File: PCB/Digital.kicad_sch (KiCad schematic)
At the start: 29 parts, among them IC1 MAX3051ESA+, J1 DE9_Pins_MountingHoles, J2 ICSP, J3 DE9_Plug_MountingHoles, J4 Conn_Coaxial, J6 Conn_01x03, J7 DOOR, J8 WINDOW, U1 PIC18F2580T-I/SO, Y2 ABLS

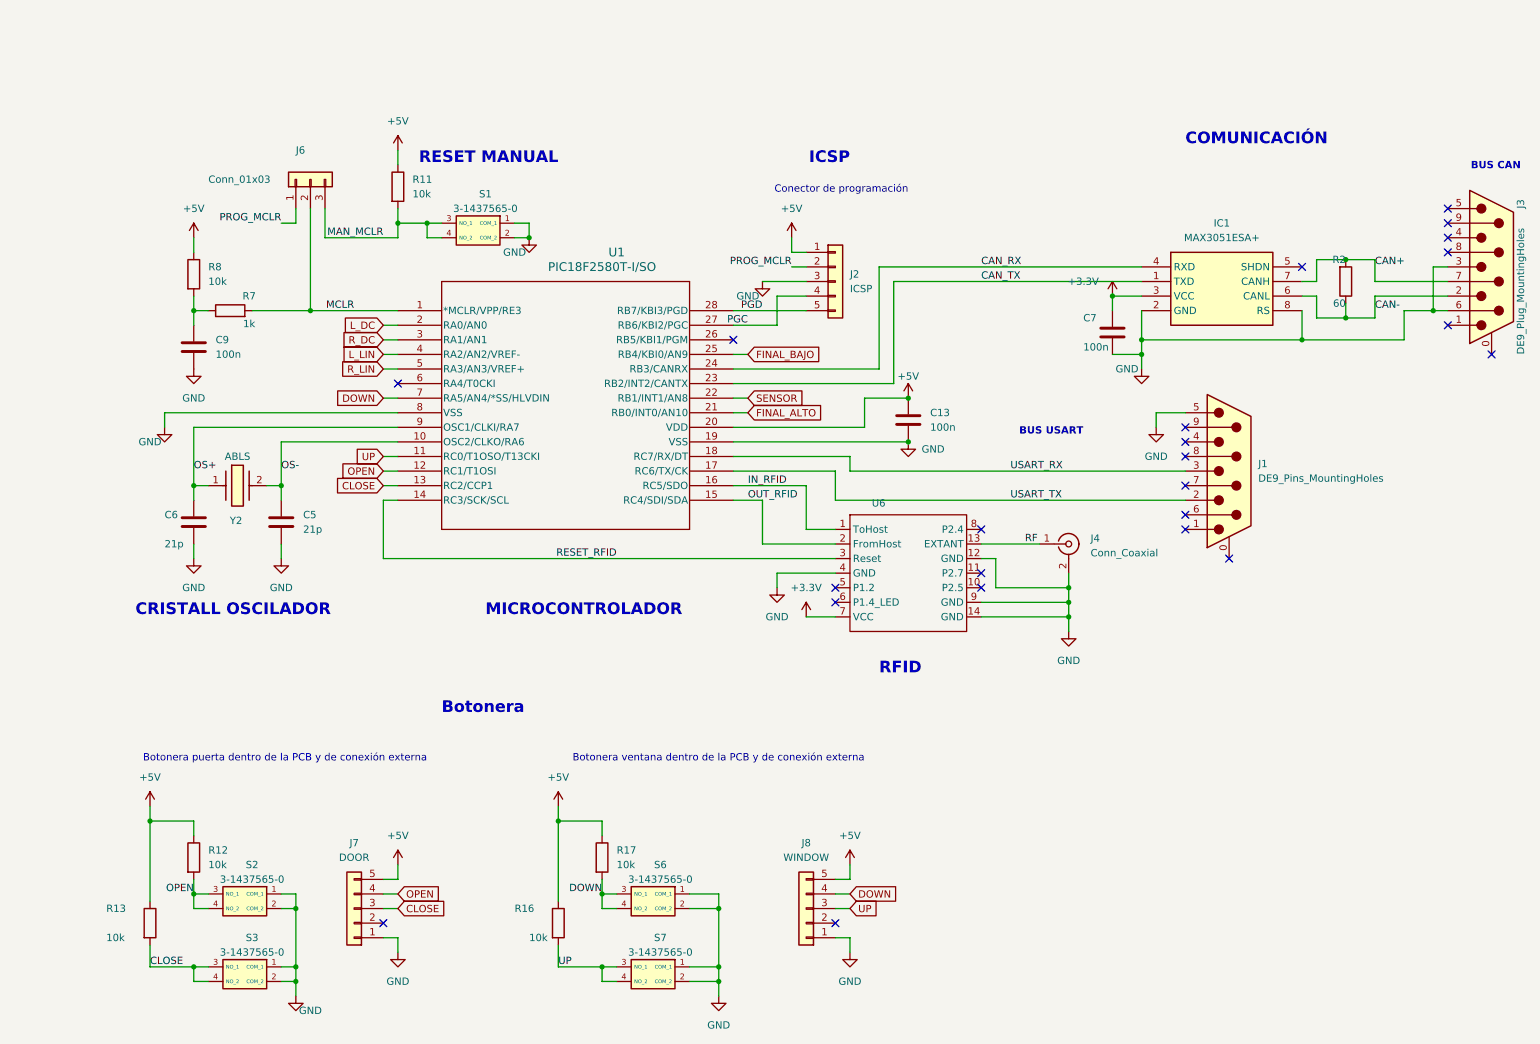
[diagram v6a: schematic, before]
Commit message: Fixed labels and ERC errors
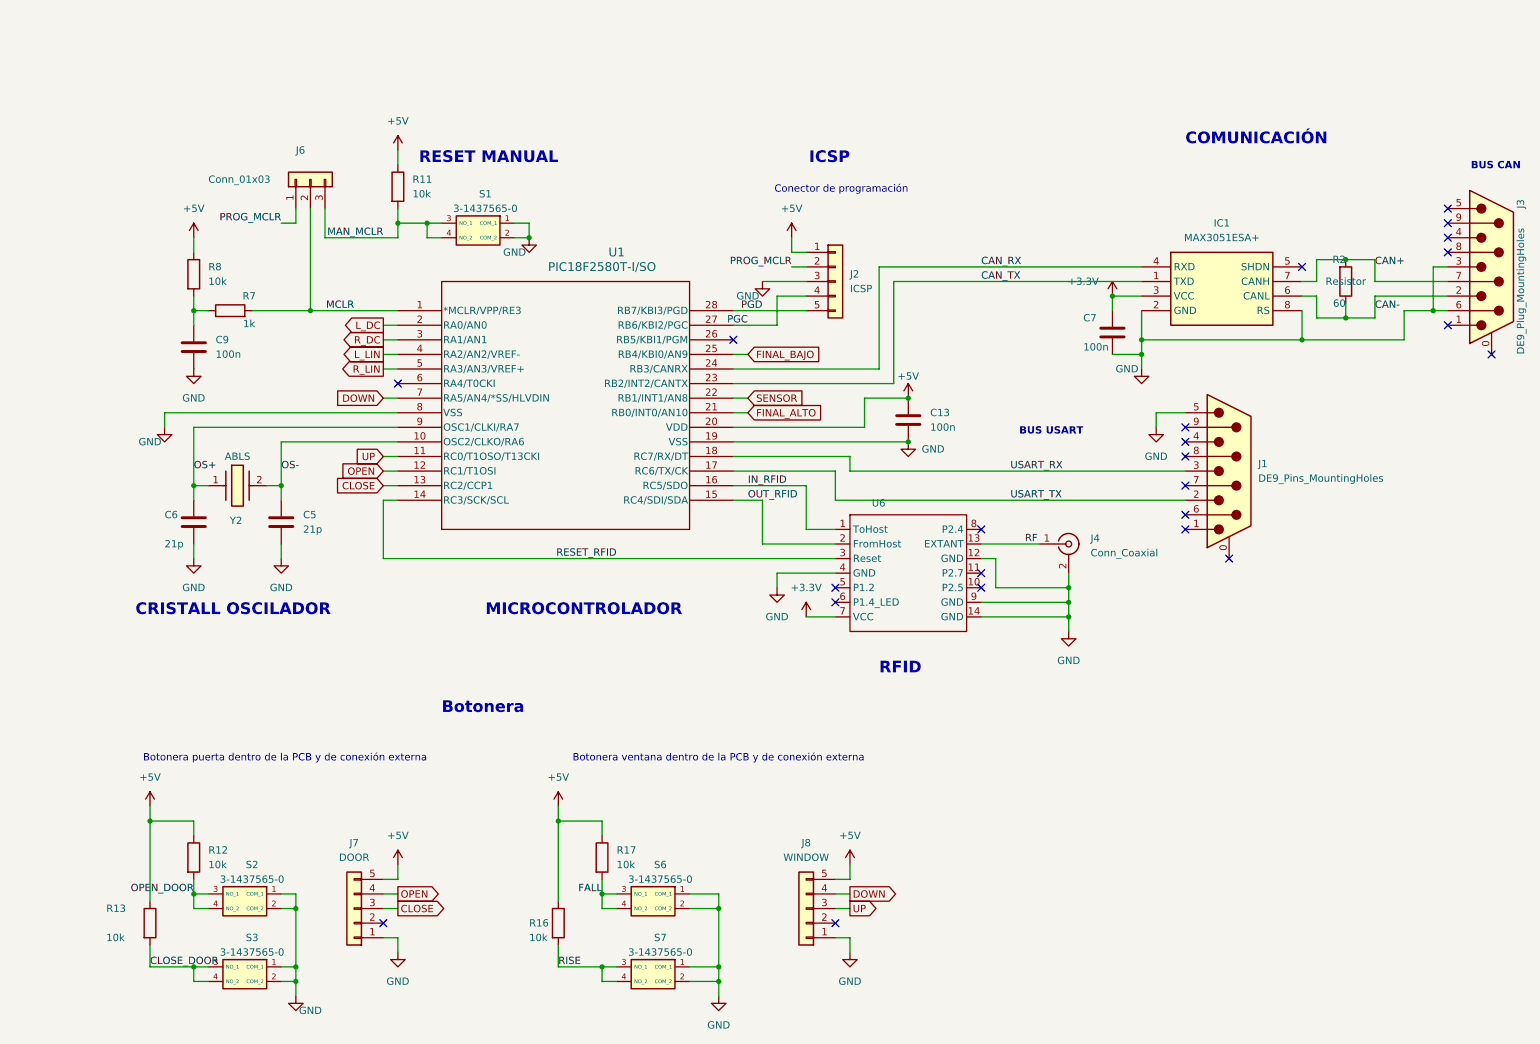
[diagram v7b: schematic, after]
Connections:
- net CLOSE: no longer R13.2, S3.3 (NO_1), S3.4 (NO_2)
- net DOWN: no longer R17.2, S6.3 (NO_1), S6.4 (NO_2)
- net OPEN: no longer R12.2, S2.3 (NO_1), S2.4 (NO_2)
- net UP: no longer R16.2, S7.3 (NO_1), S7.4 (NO_2)
- new net CLOSE_DOOR: R13.2, S3.3 (NO_1), S3.4 (NO_2)
- new net FALL: R17.2, S6.3 (NO_1), S6.4 (NO_2)
- new net OPEN_DOOR: R12.2, S2.3 (NO_1), S2.4 (NO_2)
- new net RISE: R16.2, S7.3 (NO_1), S7.4 (NO_2)
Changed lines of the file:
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@@
 		)
 	)
-	(label "UP"
+	(label "RISE"
 		(at 109.22 180.34 0)
 		(effects
@@
 		)
 	)
-	(label "OPEN"
+	(label "OPEN_DOOR"
 		(at 45.72 167.64 180)
 		(effects
@@
 		)
 	)
-	(label "DOWN"
+	(label "FALL"
 		(at 116.84 167.64 180)
 		(effects
@@
 		)
 	)
-	(label "CLOSE"
+	(label "CLOSE_DOOR"
 		(at 38.1 180.34 0)
 		(effects
@@
 	)
 	(global_label "CLOSE"
-		(shape input)
+		(shape output)
 		(at 81.28 170.18 0)
 		(fields_autoplaced yes)
@@
 	)
 	(global_label "R_DC"
-		(shape input)
+		(shape output)
 		(at 78.74 71.12 180)
 		(fields_autoplaced yes)
@@
 	)
 	(global_label "L_LIN"
-		(shape input)
+		(shape output)
 		(at 78.74 73.66 180)
 		(fields_autoplaced yes)
@@
 	)
 	(global_label "R_LIN"
-		(shape input)
+		(shape output)
 		(at 78.74 76.2 180)
 		(fields_autoplaced yes)
@@
 	)
 	(global_label "UP"
-		(shape input)
+		(shape output)
 		(at 160.02 170.18 0)
 		(fields_autoplaced yes)
@@
 	)
 	(global_label "L_DC"
-		(shape input)
+		(shape output)
 		(at 78.74 68.58 180)
 		(fields_autoplaced yes)
@@
 	)
 	(global_label "DOWN"
-		(shape input)
+		(shape output)
 		(at 160.02 167.64 0)
 		(fields_autoplaced yes)
@@
 	)
 	(global_label "OPEN"
-		(shape input)
+		(shape output)
 		(at 81.28 167.64 0)
 		(fields_autoplaced yes)
@@
 	)
 	(symbol
-		(lib_name "GND_6")
 		(lib_id "power:GND")
 		(at 144.78 60.96 0)
@@
 	)
 	(symbol
-		(lib_name "GND_4")
 		(lib_id "power:GND")
 		(at 198.12 121.92 0)
@@
 			)
 		)
-		(property "Description" ""
+		(property "Description" "Power symbol creates a global label with name \"GND\" , ground"
 			(at 40.64 86.36 0)
 			(effects
@@
 					(size 1.27 1.27)
 				)
+				(hide yes)
 			)
 		)
@@
 			)
 		)
-		(property "Description" ""
+		(property "Description" "Resistor"
 			(at 246.38 60.96 0)
 			(effects
@@
 	)
 	(symbol
-		(lib_name "+5V_1")
 		(lib_id "power:+5V")
 		(at 81.28 162.56 0)
@@
 		(dnp no)
 		(property "Reference" "R16"
-			(at 101.6 170.18 0)
+			(at 104.14 172.72 0)
 			(effects
 				(font
@@
 	)
 	(symbol
-		(lib_name "GND_3")
 		(lib_id "power:GND")
 		(at 213.36 86.36 0)
@@
 	)
 	(symbol
-		(lib_name "GND_5")
 		(lib_id "power:GND")
 		(at 137.16 185.42 0)
@@
 	)
 	(symbol
-		(lib_name "GND_5")
 		(lib_id "power:GND")
 		(at 81.28 177.8 0)
@@
 	)
 	(symbol
-		(lib_name "+5V_1")
 		(lib_id "power:+5V")
 		(at 160.02 162.56 0)
@@
 	)
 	(symbol
-		(lib_name "+5V_1")
 		(lib_id "power:+5V")
 		(at 109.22 152.4 0)
@@
 	)
 	(symbol
-		(lib_name "GND_4")
 		(lib_id "power:GND")
 		(at 147.32 114.3 0)
@@
 	)
 	(symbol
-		(lib_name "GND_1")
 		(lib_id "power:GND")
 		(at 45.72 109.22 0)
@@
 	)
 	(symbol
-		(lib_name "GND_5")
 		(lib_id "power:GND")
 		(at 63.5 185.42 0)
@@
 			)
 		)
-		(property "Description" ""
-			(at 170.18 88.9 0)
+		(property "Description" "Power symbol creates a global label with name \"GND\" , ground"
+			(at 180.34 81.28 0)
 			(effects
 				(font
 					(size 1.27 1.27)
 				)
+				(hide yes)
 			)
 		)
@@
 			)
 		)
-		(property "Description" ""
-			(at 170.18 81.28 0)
+		(property "Description" "Power symbol creates a global label with name \"+5V\""
+			(at 182.88 76.2 0)
 			(effects
 				(font
 					(size 1.27 1.27)
 				)
+				(hide yes)
 			)
 		)
@@
 	)
 	(symbol
-		(lib_name "+5V_2")
 		(lib_id "power:+5V")
 		(at 149.86 53.34 0)
@@
 	)
 	(symbol
-		(lib_name "GND_5")
 		(lib_id "power:GND")
 		(at 160.02 177.8 0)
@@
 	)
 	(symbol
-		(lib_name "GND_2")
 		(lib_id "power:GND")
 		(at 45.72 76.2 0)
@@
 	)
 	(symbol
-		(lib_name "GND_1")
 		(lib_id "power:GND")
 		(at 60.96 109.22 0)
@@
 			)
 		)
-		(property "Description" ""
-			(at 210.82 76.2 0)
+		(property "Description" "Power symbol creates a global label with name \"GND\" , ground"
+			(at 236.22 78.74 0)
 			(effects
 				(font
 					(size 1.27 1.27)
 				)
+				(hide yes)
 			)
 		)
@@
 	)
 	(symbol
-		(lib_name "+5V_1")
 		(lib_id "power:+5V")
 		(at 38.1 152.4 0)

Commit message: ADDED footprint RFID lector
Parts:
- U6: footprint DLP-RFID2:DLP-RFID2 -> CREATED:DLP-RFID2
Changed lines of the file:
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@@
 			)
 		)
-		(property "Footprint" "DLP-RFID2:DLP-RFID2"
+		(property "Footprint" "CREATED:DLP-RFID2"
 			(at 157.48 104.14 0)
 			(effects
@@
 			)
 		)
-		(property "Datasheet" ""
+		(property "Datasheet" "https://www.mouser.es/datasheet/2/117/dlp-rfid2-ds-v114-1374531.pdf"
 			(at 149.86 104.14 0)
 			(effects
